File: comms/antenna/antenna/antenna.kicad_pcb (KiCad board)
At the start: 2 copper layers, 25.4 x 29.5 mm, 3 parts, among them J1 Conn_01x03

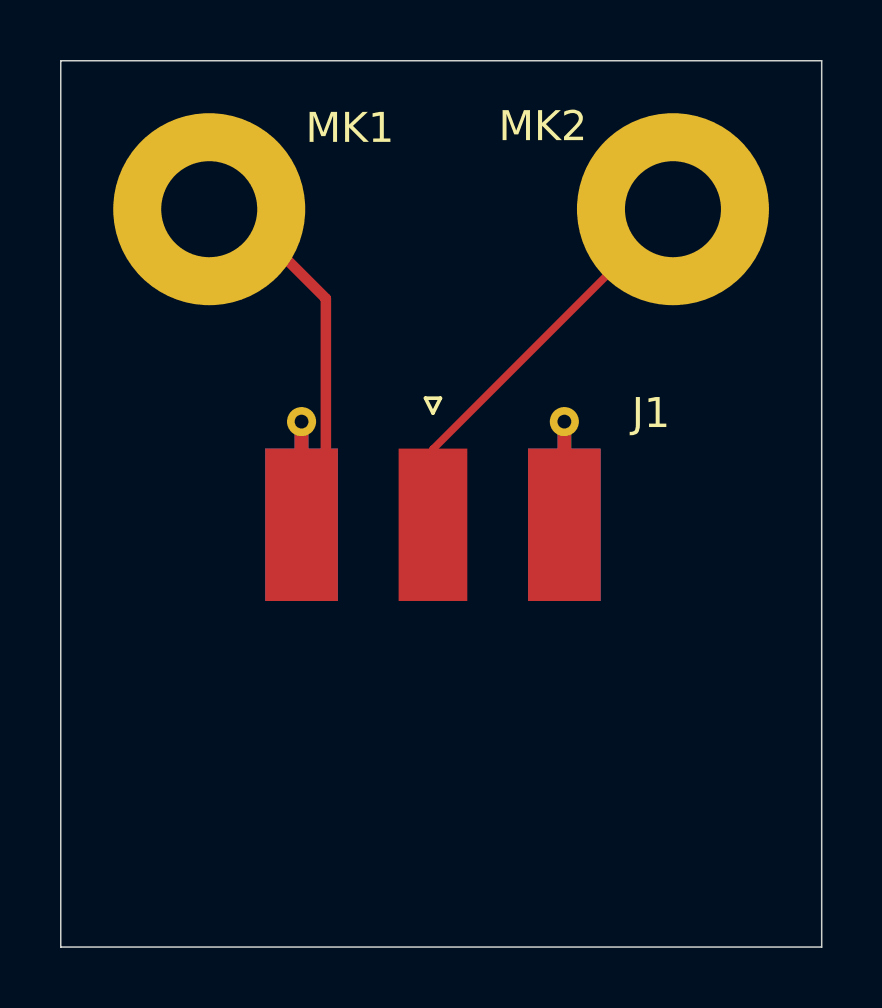
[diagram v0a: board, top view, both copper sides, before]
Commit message: Fixed board size
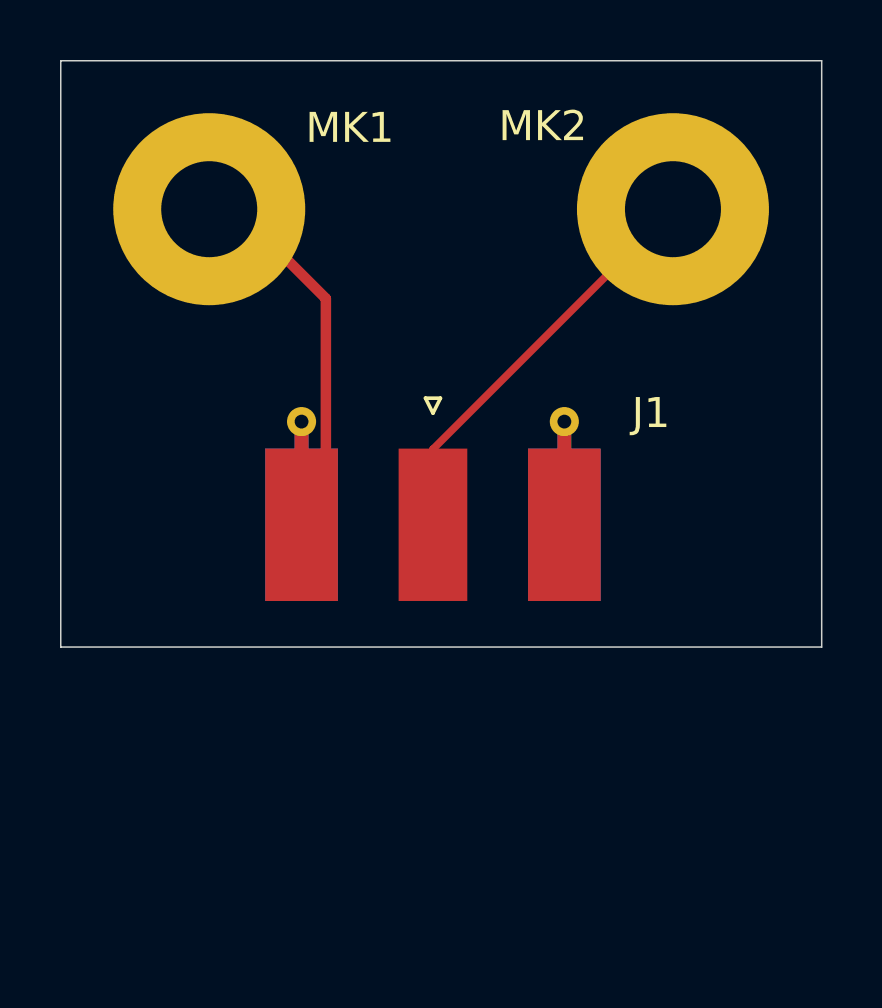
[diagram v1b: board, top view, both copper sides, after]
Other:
- board size 25.4 x 29.5 mm -> 25.4 x 19.5 mm
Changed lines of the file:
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@@
     )
   )
-  (gr_line (start 162.95764 135.79488) (end 137.59294 135.79488) (layer Edge.Cuts) (width 0.05))
-  (gr_line (start 162.95764 106.25188) (end 162.95764 135.79488) (layer Edge.Cuts) (width 0.05))
+  (gr_line (start 162.95764 125.79488) (end 137.59294 125.79488) (layer Edge.Cuts) (width 0.05))
+  (gr_line (start 162.95764 106.25188) (end 162.95764 125.79488) (layer Edge.Cuts) (width 0.05))
   (gr_line (start 162.95764 106.25188) (end 137.59294 106.25188) (layer Edge.Cuts) (width 0.05))
-  (gr_line (start 137.59294 106.25188) (end 137.59294 135.79488) (layer Edge.Cuts) (width 0.05))
+  (gr_line (start 137.59294 106.25188) (end 137.59294 125.79488) (layer Edge.Cuts) (width 0.05))
   (dimension 3.03022 (width 0.15) (layer Dwgs.User)
     (gr_text "3.00 mm" (at 144.01927 103.3607) (layer Dwgs.User)
